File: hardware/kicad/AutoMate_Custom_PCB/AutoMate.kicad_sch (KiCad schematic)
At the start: 71 parts, among them J1 8P8C, J11_Doorsensor1 Conn_01x02_Socket, J12_ZMCT103C1 Conn_01x02_Socket, J2_BH1750 Conn_01x05_Socket, J2_IR_AHT_BH17 Conn_01x05_Socket, J2_IR_AHT_BH18 Conn_01x05_Socket, J2_PCA9685_Female1 PCA9685, J2_PCA9685_Male1 PCA9685, J5_Relay1 Relay, J9_AHT_BMP1 Conn_01x04_Socket, J9_ZMPT1 Conn_01x04_Socket, SW1_Manual_Override1 SW_DIP_x12, T1 Screw_Terminal_01x02, T10 ST01x02, T11 ST01x02, T12 ST01x02, T13 ST01x02, T14 ST01x02, T15 ST01x02, T2 Screw_Terminal_01x02, T3 Screw_Terminal_01x02, T4 Screw_Terminal_01x02, T5 Screw_Terminal_01x02, T6 Screw_Terminal_01x02, T7 Screw_Terminal_01x02, T8 ST01x02, T9 ST01x02, U1 815, U1_ESP32-DEVKITC1 ESP32-DEVKITC, U2_74HC595 74HC595

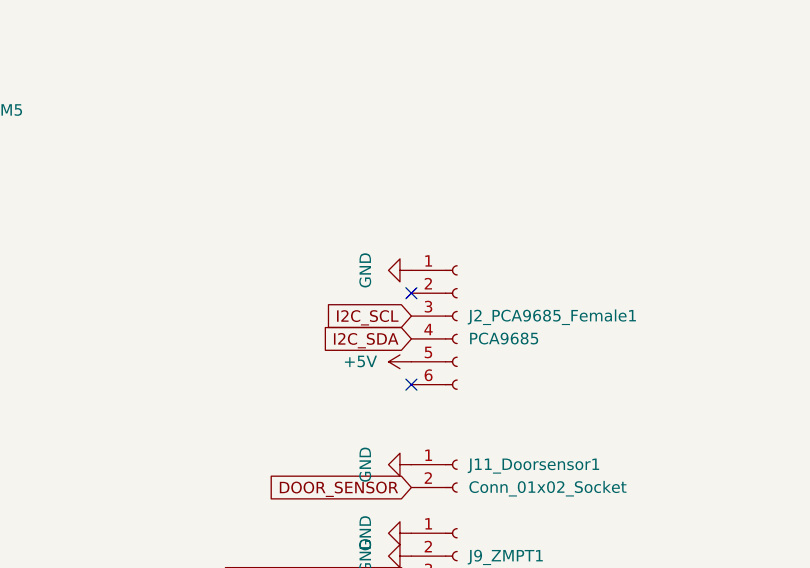
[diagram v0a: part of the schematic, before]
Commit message: v1.0.3: Fix 12V driver automation and state persistence
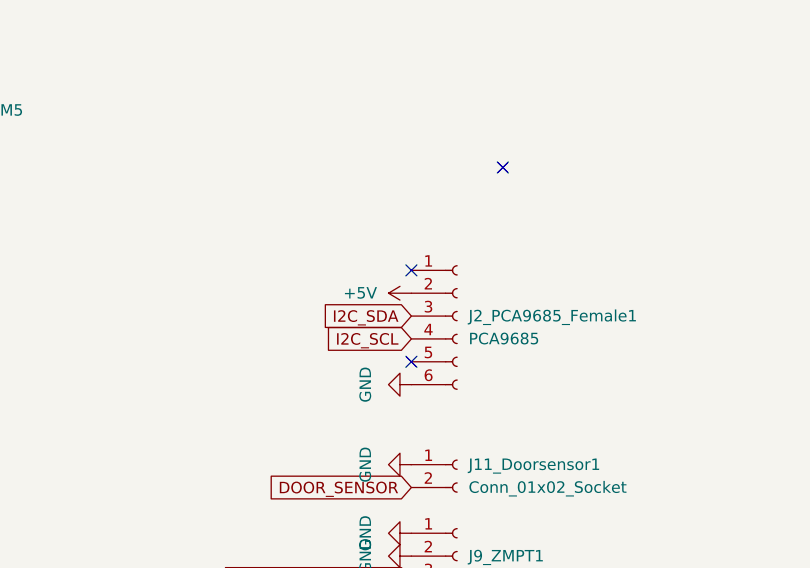
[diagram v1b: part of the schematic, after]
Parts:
- J2_PCA9685_Female1: footprint Connector_PinHeader_2.54mm:PinHeader_1x06_P2.54mm_Horizontal -> Connector_PinSocket_2.54mm:PinSocket_1x06_P2.54mm_Horizontal
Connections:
- net +5V: now also J2_PCA9685_Female1.2 (Pin_2); no longer J2_PCA9685_Female1.5 (Pin_5)
- net GND: now also J2_PCA9685_Female1.6 (Pin_6); no longer J2_PCA9685_Female1.1 (Pin_1)
- net I2C_SCL: now also J2_PCA9685_Female1.4 (Pin_4); no longer J2_PCA9685_Female1.3 (Pin_3)
- net I2C_SDA: now also J2_PCA9685_Female1.3 (Pin_3); no longer J2_PCA9685_Female1.4 (Pin_4)
- no-connect marks 26 -> 27
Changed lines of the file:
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@@
 	)
 	(no_connect
-		(at 180.34 109.22)
-	)
-	(no_connect
 		(at 50.8 265.43)
 	)
@@
 	)
 	(no_connect
+		(at 180.34 106.68)
+	)
+	(no_connect
 		(at 193.04 243.84)
 	)
@@
 	)
 	(no_connect
+		(at 180.34 96.52)
+	)
+	(no_connect
 		(at 426.72 22.86)
 	)
@@
 	)
 	(no_connect
-		(at 180.34 99.06)
+		(at 190.5 85.09)
 	)
 	(no_connect
@@
 		)
 	)
-	(global_label "I2C_SDA"
-		(shape input)
-		(at 180.34 104.14 180)
-		(fields_autoplaced yes)
-		(effects
-			(font
-				(size 1.27 1.27)
-			)
-			(justify right)
-		)
-		(property "Intersheetrefs" "${INTERSHEET_REFS}"
-			(at 169.7348 104.14 0)
-			(hide yes)
-			(show_name no)
-			(do_not_autoplace no)
-			(effects
-				(font
-					(size 1.27 1.27)
-				)
-				(justify right)
-			)
-		)
-	)
 	(global_label "PSL"
 		(shape input)
@@
 		)
 	)
+	(global_label "I2C_SCL"
+		(shape input)
+		(at 180.34 104.14 180)
+		(fields_autoplaced yes)
+		(effects
+			(font
+				(size 1.27 1.27)
+			)
+			(justify right)
+		)
+		(property "Intersheetrefs" "${INTERSHEET_REFS}"
+			(at 169.7953 104.14 0)
+			(hide yes)
+			(show_name no)
+			(do_not_autoplace no)
+			(effects
+				(font
+					(size 1.27 1.27)
+				)
+				(justify right)
+			)
+		)
+	)
 	(global_label "M3B"
 		(shape input)
@@
 		)
 	)
-	(global_label "I2C_SCL"
+	(global_label "MONITOR4_BACKLIGHT"
 		(shape input)
-		(at 180.34 101.6 180)
+		(at 320.04 160.02 270)
 		(fields_autoplaced yes)
 		(effects
@@
 		)
 		(property "Intersheetrefs" "${INTERSHEET_REFS}"
-			(at 169.7953 101.6 0)
+			(at 320.04 183.5672 90)
 			(hide yes)
 			(show_name no)
@@
 		)
 	)
-	(global_label "MONITOR4_BACKLIGHT"
+	(global_label "CBL"
 		(shape input)
-		(at 320.04 160.02 270)
+		(at 415.29 55.88 270)
 		(fields_autoplaced yes)
 		(effects
@@
 		)
 		(property "Intersheetrefs" "${INTERSHEET_REFS}"
-			(at 320.04 183.5672 90)
+			(at 415.29 62.4333 90)
 			(hide yes)
 			(show_name no)
@@
 		)
 	)
-	(global_label "CBL"
+	(global_label "I2C_SDA"
 		(shape input)
-		(at 415.29 55.88 270)
+		(at 180.34 160.02 180)
 		(fields_autoplaced yes)
 		(effects
@@
 		)
 		(property "Intersheetrefs" "${INTERSHEET_REFS}"
-			(at 415.29 62.4333 90)
+			(at 169.7348 160.02 0)
 			(hide yes)
 			(show_name no)
@@
 		)
 	)
-	(global_label "I2C_SDA"
+	(global_label "MONITOR2_BACKLIGHT"
 		(shape input)
-		(at 180.34 160.02 180)
+		(at 342.9 83.82 270)
 		(fields_autoplaced yes)
 		(effects
@@
 		)
 		(property "Intersheetrefs" "${INTERSHEET_REFS}"
-			(at 169.7348 160.02 0)
+			(at 342.9 107.3672 90)
 			(hide yes)
 			(show_name no)
@@
 		)
 	)
-	(global_label "MONITOR2_BACKLIGHT"
+	(global_label "I2C_SDA"
 		(shape input)
-		(at 342.9 83.82 270)
+		(at 180.34 101.6 180)
 		(fields_autoplaced yes)
 		(effects
@@
 		)
 		(property "Intersheetrefs" "${INTERSHEET_REFS}"
-			(at 342.9 107.3672 90)
+			(at 169.7348 101.6 0)
 			(hide yes)
 			(show_name no)
@@
 	)
 	(symbol
-		(lib_id "power:+5V")
-		(at 180.34 106.68 90)
-		(unit 1)
-		(body_style 1)
-		(exclude_from_sim no)
-		(in_bom yes)
-		(on_board yes)
-		(in_pos_files yes)
-		(dnp no)
-		(fields_autoplaced yes)
-		(property "Reference" "#PWR020"
-			(at 184.15 106.68 0)
-			(hide yes)
-			(show_name no)
-			(do_not_autoplace no)
-			(effects
-				(font
-					(size 1.27 1.27)
-				)
-			)
-		)
-		(property "Value" "+5V"
-			(at 176.53 106.6799 90)
-			(show_name no)
-			(do_not_autoplace no)
-			(effects
-				(font
-					(size 1.27 1.27)
-				)
-				(justify left)
-			)
-		)
-		(property "Footprint" ""
-			(at 180.34 106.68 0)
-			(hide yes)
-			(show_name no)
-			(do_not_autoplace no)
-			(effects
-				(font
-					(size 1.27 1.27)
-				)
-			)
-		)
-		(property "Datasheet" ""
-			(at 180.34 106.68 0)
-			(hide yes)
-			(show_name no)
-			(do_not_autoplace no)
-			(effects
-				(font
-					(size 1.27 1.27)
-				)
-			)
-		)
-		(property "Description" "Power symbol creates a global label with name \"+5V\""
-			(at 180.34 106.68 0)
-			(hide yes)
-			(show_name no)
-			(do_not_autoplace no)
-			(effects
-				(font
-					(size 1.27 1.27)
-				)
-			)
-		)
-		(pin "1"
-		)
-		(instances
-			(project "AutoMate"
-				(path "/6e78f634-a06d-4f9f-a273-756e182159e5"
-					(reference "#PWR020")
-					(unit 1)
-				)
-			)
-		)
-	)
-	(symbol
 		(lib_name "Dual MOSFET Trigger Switch Module_1")
 		(lib_id "D4184 V1.0:Dual MOSFET Trigger Switch Module")
@@
 	)
 	(symbol
+		(lib_id "power:+5V")
+		(at 180.34 99.06 90)
+		(unit 1)
+		(body_style 1)
+		(exclude_from_sim no)
+		(in_bom yes)
+		(on_board yes)
+		(in_pos_files yes)
+		(dnp no)
+		(fields_autoplaced yes)
+		(property "Reference" "#PWR020"
+			(at 184.15 99.06 0)
+			(hide yes)
+			(show_name no)
+			(do_not_autoplace no)
+			(effects
+				(font
+					(size 1.27 1.27)
+				)
+			)
+		)
+		(property "Value" "+5V"
+			(at 176.53 99.0599 90)
+			(show_name no)
+			(do_not_autoplace no)
+			(effects
+				(font
+					(size 1.27 1.27)
+				)
+				(justify left)
+			)
+		)
+		(property "Footprint" ""
+			(at 180.34 99.06 0)
+			(hide yes)
+			(show_name no)
+			(do_not_autoplace no)
+			(effects
+				(font
+					(size 1.27 1.27)
+				)
+			)
+		)
+		(property "Datasheet" ""
+			(at 180.34 99.06 0)
+			(hide yes)
+			(show_name no)
+			(do_not_autoplace no)
+			(effects
+				(font
+					(size 1.27 1.27)
+				)
+			)
+		)
+		(property "Description" "Power symbol creates a global label with name \"+5V\""
+			(at 180.34 99.06 0)
+			(hide yes)
+			(show_name no)
+			(do_not_autoplace no)
+			(effects
+				(font
+					(size 1.27 1.27)
+				)
+			)
+		)
+		(pin "1"
+		)
+		(instances
+			(project "AutoMate"
+				(path "/6e78f634-a06d-4f9f-a273-756e182159e5"
+					(reference "#PWR020")
+					(unit 1)
+				)
+			)
+		)
+	)
+	(symbol
 		(lib_id "power:GND")
 		(at 302.26 160.02 0)
@@
 			)
 		)
-		(property "Footprint" "Connector_PinHeader_2.54mm:PinHeader_1x06_P2.54mm_Horizontal"
+		(property "Footprint" "Connector_PinSocket_2.54mm:PinSocket_1x06_P2.54mm_Horizontal"
 			(at 185.42 101.6 0)
 			(hide yes)
@@
 	(symbol
 		(lib_id "power:GND")
-		(at 180.34 96.52 270)
+		(at 180.34 109.22 270)
 		(unit 1)
 		(body_style 1)
@@
 		(dnp no)
 		(property "Reference" "#PWR012"
-			(at 173.99 96.52 0)
+			(at 173.99 109.22 0)
 			(hide yes)
 			(show_name no)
@@
 		)
 		(property "Value" "GND"
-			(at 175.26 96.52 0)
+			(at 175.26 109.22 0)
 			(show_name no)
 			(do_not_autoplace no)
@@
 		)
 		(property "Footprint" ""
-			(at 180.34 96.52 0)
+			(at 180.34 109.22 0)
 			(hide yes)
 			(show_name no)
@@
 		)
 		(property "Datasheet" ""
-			(at 180.34 96.52 0)
+			(at 180.34 109.22 0)
 			(hide yes)
 			(show_name no)
@@
 		)
 		(property "Description" "Power symbol creates a global label with name \"GND\" , ground"
-			(at 180.34 96.52 0)
+			(at 180.34 109.22 0)
 			(hide yes)
 			(show_name no)

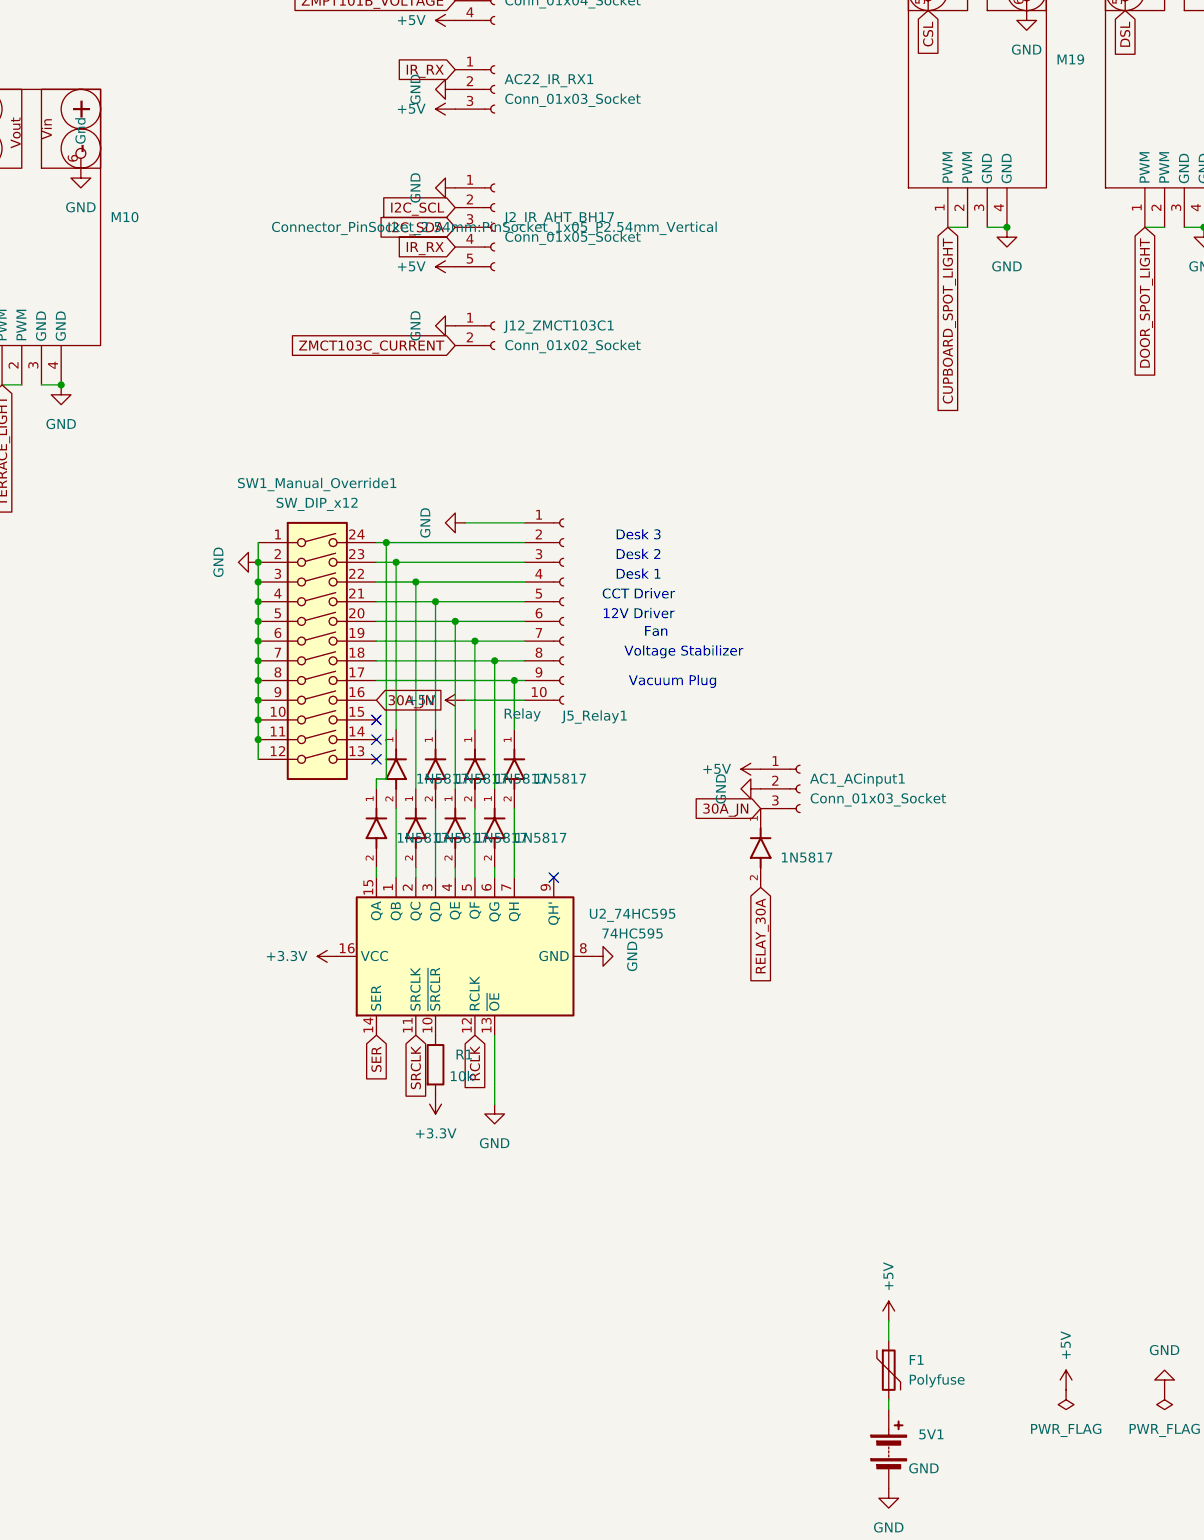
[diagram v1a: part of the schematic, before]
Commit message: deploy: v1.0.5 - Fixed 12V driver restart race condition, added restart API service
- Fixed 12V driver race condition on boot: now restores lights first, then sets 12V driver based on actual light states
- Removed invalid 'await 500ms' and 'light_desk3' references from on_boot lambda
- Fixed light state checks to use .current_values.is_on() API
- Added restart API service accessible via Home Assistant
- Uses esp_restart() for clean restart that preserves state
- All globals have restore_value: yes for state persistence
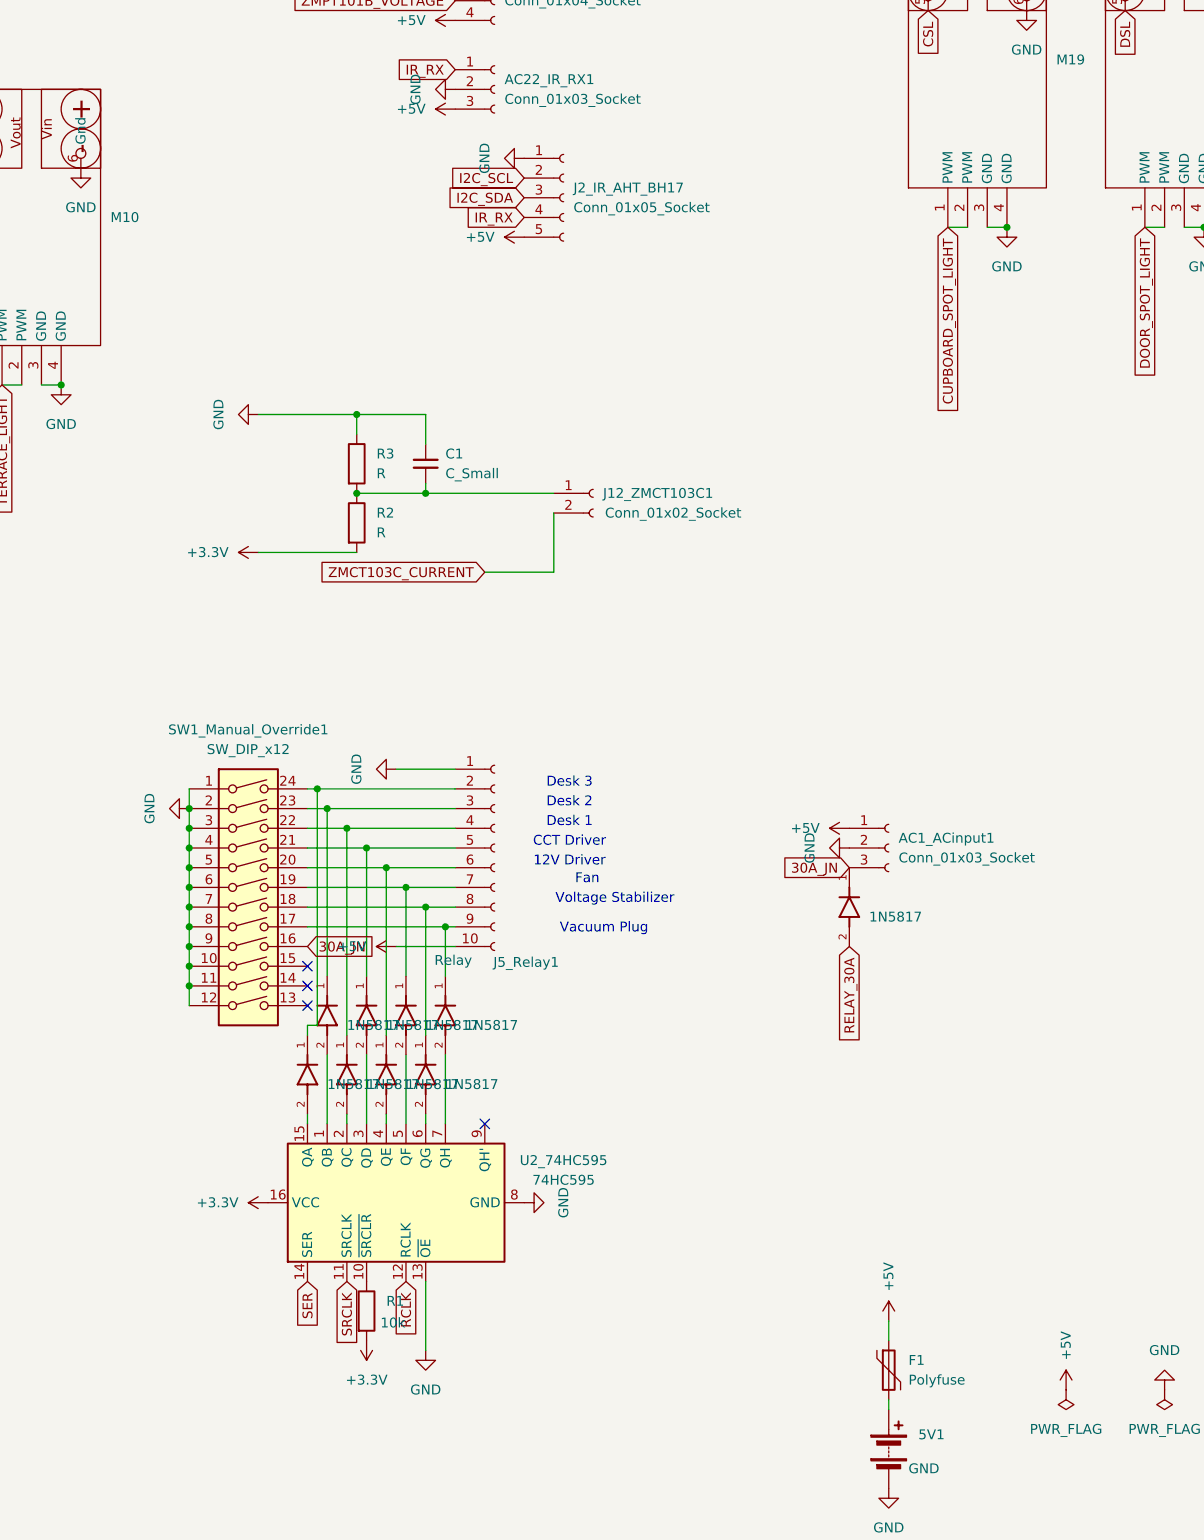
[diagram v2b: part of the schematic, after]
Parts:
- added C1: C_Small, Capacitor_THT:C_Disc_D3.0mm_W2.0mm_P2.50mm, symbol Device:C_Small
- added R2, R3: R, Resistor_THT:R_Axial_DIN0411_L9.9mm_D3.6mm_P5.08mm_Vertical, symbol Device:R
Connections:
- net +3.3V: now also R2.2
- net GND: now also C1.1, R3.1; no longer J12_ZMCT103C1.1 (Pin_1)
- new net: C1.2, J12_ZMCT103C1.1 (Pin_1), R2.1, R3.2
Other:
- moved on the sheet: AC1_ACinput1, J12_ZMCT103C1, J2_IR_AHT_BH17, J5_Relay1, R1, SW1_Manual_Override1, U2_74HC595
